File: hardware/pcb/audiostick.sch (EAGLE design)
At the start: 65 parts, among them IC1 TPS73633MBDV, IC3 PCM5102ASW, IC5 AP22804W5, IC6 TINY13V-10SSU, J2 AUDIO_JACK_3.5MM_PTH, J3 USB-B, SW1 EVQP7, T1 BC850

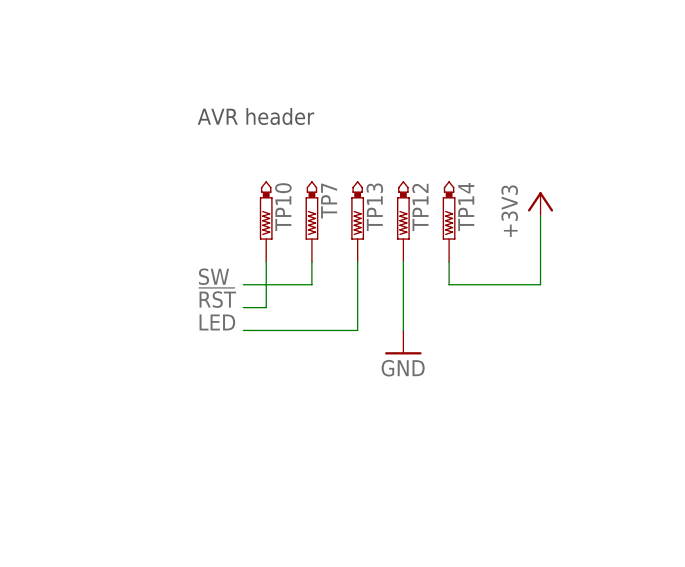
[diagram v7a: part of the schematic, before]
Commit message: Changed pogo points for proper header, silly idea!
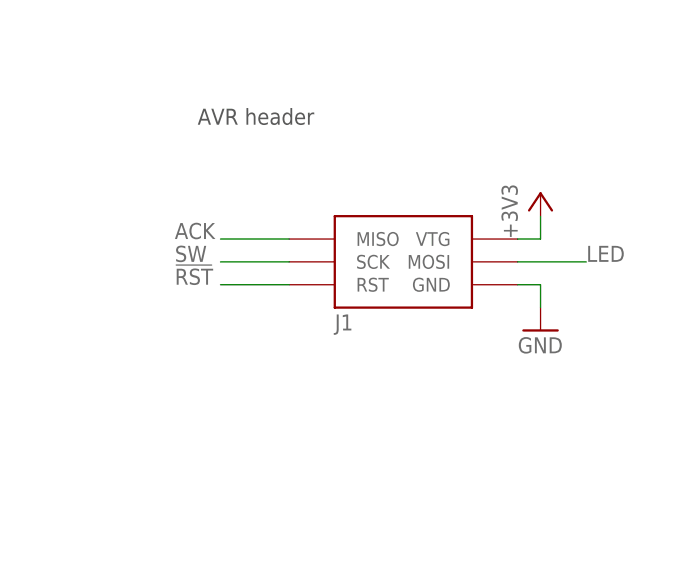
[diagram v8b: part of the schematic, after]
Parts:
- removed TP10, TP12, TP13, TP14, TP7: PTR1TP08R, testpad:PTR1TP08R
- added J1: AVRISP6TH127, AWJLEagleLib:AVRISP6TH127
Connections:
- net !RST: now also J1.RST; no longer TP10.TP
- net +3V3: now also J1.VTG; no longer TP14.TP
- net ACK: now also J1.MISO
- net GND: now also J1.GND; no longer TP12.TP
- net LED: now also J1.MOSI; no longer TP13.TP
- net SW: now also J1.SCK; no longer TP7.TP
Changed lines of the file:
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@@
 <part name="R13" library="rcl" library_urn="urn:adsk.eagle:library:334" deviceset="R-EU_" device="R0603" package3d_urn="urn:adsk.eagle:package:23555/3" value="10K"/>
 <part name="IC6" library="atmel" library_urn="urn:adsk.eagle:library:105" deviceset="TINY13" device="SSU" package3d_urn="urn:adsk.eagle:package:4358/1" technology="V-10"/>
-<part name="+3V5" library="supply1" library_urn="urn:adsk.eagle:library:371" deviceset="+3V3" device=""/>
-<part name="GND19" library="supply1" library_urn="urn:adsk.eagle:library:371" deviceset="GND" device=""/>
 <part name="TP1" library="testpad" library_urn="urn:adsk.eagle:library:385" deviceset="PTR1" device="PAD1-13" package3d_urn="urn:adsk.eagle:package:27946/1"/>
 <part name="TP2" library="testpad" library_urn="urn:adsk.eagle:library:385" deviceset="PTR1" device="PAD1-13" package3d_urn="urn:adsk.eagle:package:27946/1"/>
@@
 <part name="R8" library="rcl" library_urn="urn:adsk.eagle:library:334" deviceset="R-EU_" device="R0603" package3d_urn="urn:adsk.eagle:package:23555/3" value="0R"/>
 <part name="SW1" library="AudioStick" deviceset="EVQP7" device=""/>
-<part name="TP7" library="testpad" library_urn="urn:adsk.eagle:library:385" deviceset="PTR1" device="TP08R" package3d_urn="urn:adsk.eagle:package:27956/1" value="PTR1TP08R"/>
-<part name="TP10" library="testpad" library_urn="urn:adsk.eagle:library:385" deviceset="PTR1" device="TP08R" package3d_urn="urn:adsk.eagle:package:27956/1" value="PTR1TP08R"/>
-<part name="TP12" library="testpad" library_urn="urn:adsk.eagle:library:385" deviceset="PTR1" device="TP08R" package3d_urn="urn:adsk.eagle:package:27956/1" value="PTR1TP08R"/>
-<part name="TP13" library="testpad" library_urn="urn:adsk.eagle:library:385" deviceset="PTR1" device="TP08R" package3d_urn="urn:adsk.eagle:package:27956/1" value="PTR1TP08R"/>
-<part name="TP14" library="testpad" library_urn="urn:adsk.eagle:library:385" deviceset="PTR1" device="TP08R" package3d_urn="urn:adsk.eagle:package:27956/1" value="PTR1TP08R"/>
+<part name="J1" library="AWJLEagleLib" deviceset="AVRISP6" device="TH127"/>
+<part name="+3V7" library="supply1" library_urn="urn:adsk.eagle:library:371" deviceset="+3V3" device=""/>
+<part name="GND28" library="supply1" library_urn="urn:adsk.eagle:library:371" deviceset="GND" device=""/>
 </parts>
 <sheets>
@@
 <attribute name="VALUE" x="55.88" y="327.66" size="1.778" layer="96" rot="MR0"/>
 </instance>
-<instance part="+3V5" gate="G$1" x="238.76" y="353.06" smashed="yes">
-<attribute name="VALUE" x="236.22" y="347.98" size="1.778" layer="96" rot="R90"/>
-</instance>
-<instance part="GND19" gate="1" x="223.52" y="335.28" smashed="yes">
-<attribute name="VALUE" x="220.98" y="332.74" size="1.778" layer="96"/>
-</instance>
 <instance part="TP1" gate="G$1" x="147.32" y="88.9" smashed="yes" rot="R90">
 <attribute name="NAME" x="153.67" y="87.884" size="1.778" layer="95" rot="R180"/>
@@
 <attribute name="VALUE" x="80.01" y="325.755" size="1.778" layer="96" rot="R90"/>
 </instance>
-<instance part="TP7" gate="G$1" x="213.36" y="347.98" smashed="yes" rot="R180">
-<attribute name="NAME" x="214.376" y="354.33" size="1.778" layer="95" rot="R270"/>
-<attribute name="TP_SIGNAL_NAME" x="212.09" y="350.52" size="1.778" layer="97" rot="R180"/>
-</instance>
-<instance part="TP10" gate="G$1" x="208.28" y="347.98" smashed="yes" rot="R180">
-<attribute name="NAME" x="209.296" y="354.33" size="1.778" layer="95" rot="R270"/>
-<attribute name="TP_SIGNAL_NAME" x="207.01" y="350.52" size="1.778" layer="97" rot="R180"/>
-</instance>
-<instance part="TP12" gate="G$1" x="223.52" y="347.98" smashed="yes" rot="R180">
-<attribute name="NAME" x="224.536" y="354.33" size="1.778" layer="95" rot="R270"/>
-<attribute name="TP_SIGNAL_NAME" x="222.25" y="350.52" size="1.778" layer="97" rot="R180"/>
-</instance>
-<instance part="TP13" gate="G$1" x="218.44" y="347.98" smashed="yes" rot="R180">
-<attribute name="NAME" x="219.456" y="354.33" size="1.778" layer="95" rot="R270"/>
-<attribute name="TP_SIGNAL_NAME" x="217.17" y="350.52" size="1.778" layer="97" rot="R180"/>
-</instance>
-<instance part="TP14" gate="G$1" x="228.6" y="347.98" smashed="yes" rot="R180">
-<attribute name="NAME" x="229.616" y="354.33" size="1.778" layer="95" rot="R270"/>
-<attribute name="TP_SIGNAL_NAME" x="227.33" y="350.52" size="1.778" layer="97" rot="R180"/>
+<instance part="J1" gate="G$1" x="223.52" y="345.44" smashed="yes">
+<attribute name="NAME" x="215.9" y="337.82" size="1.778" layer="95"/>
+</instance>
+<instance part="+3V7" gate="G$1" x="238.76" y="353.06" smashed="yes">
+<attribute name="VALUE" x="236.22" y="347.98" size="1.778" layer="96" rot="R90"/>
+</instance>
+<instance part="GND28" gate="1" x="238.76" y="337.82" smashed="yes">
+<attribute name="VALUE" x="236.22" y="335.28" size="1.778" layer="96"/>
 </instance>
 </instances>
@@
 </segment>
 <segment>
-<pinref part="GND19" gate="1" pin="GND"/>
-<pinref part="TP12" gate="G$1" pin="TP"/>
-<wire x1="223.52" y1="337.82" x2="223.52" y2="345.44" width="0.1524" layer="91"/>
-</segment>
-<segment>
 <pinref part="TP8" gate="G$1" pin="TP"/>
 <wire x1="139.7" y1="40.64" x2="139.7" y2="38.1" width="0.1524" layer="91"/>
@@
 <wire x1="129.54" y1="335.28" x2="129.54" y2="337.82" width="0.1524" layer="91"/>
 </segment>
+<segment>
+<pinref part="J1" gate="G$1" pin="GND"/>
+<pinref part="GND28" gate="1" pin="GND"/>
+<wire x1="236.22" y1="342.9" x2="238.76" y2="342.9" width="0.1524" layer="91"/>
+<wire x1="238.76" y1="342.9" x2="238.76" y2="340.36" width="0.1524" layer="91"/>
+</segment>
 </net>
 <net name="PWR" class="0">
@@
 </segment>
 <segment>
-<pinref part="+3V5" gate="G$1" pin="+3V3"/>
-<wire x1="228.6" y1="342.9" x2="238.76" y2="342.9" width="0.1524" layer="91"/>
-<wire x1="238.76" y1="342.9" x2="238.76" y2="350.52" width="0.1524" layer="91"/>
-<pinref part="TP14" gate="G$1" pin="TP"/>
-<wire x1="228.6" y1="345.44" x2="228.6" y2="342.9" width="0.1524" layer="91"/>
-</segment>
-<segment>
 <pinref part="R14" gate="G$1" pin="2"/>
 <pinref part="+3V6" gate="G$1" pin="+3V3"/>
@@
 <wire x1="129.54" y1="375.92" x2="129.54" y2="378.46" width="0.1524" layer="91"/>
 </segment>
+<segment>
+<pinref part="J1" gate="G$1" pin="VTG"/>
+<pinref part="+3V7" gate="G$1" pin="+3V3"/>
+<wire x1="236.22" y1="347.98" x2="238.76" y2="347.98" width="0.1524" layer="91"/>
+<wire x1="238.76" y1="347.98" x2="238.76" y2="350.52" width="0.1524" layer="91"/>
+</segment>
 </net>
 <net name="!RST" class="0">
-<segment>
-<label x="200.66" y="340.36" size="1.778" layer="95"/>
-<pinref part="TP10" gate="G$1" pin="TP"/>
-<wire x1="208.28" y1="340.36" x2="205.74" y2="340.36" width="0.1524" layer="91"/>
-<wire x1="208.28" y1="345.44" x2="208.28" y2="340.36" width="0.1524" layer="91"/>
-</segment>
 <segment>
 <pinref part="IC6" gate="G$1" pin="PB5/PCINT5/!RESET!/ADC0/DW"/>
@@
 <wire x1="73.66" y1="335.28" x2="73.66" y2="358.14" width="0.1524" layer="91"/>
 <label x="76.2" y="335.28" size="1.778" layer="95"/>
+</segment>
+<segment>
+<pinref part="J1" gate="G$1" pin="RST"/>
+<wire x1="210.82" y1="342.9" x2="203.2" y2="342.9" width="0.1524" layer="91"/>
+<label x="198.12" y="342.9" size="1.778" layer="95"/>
 </segment>
 </net>
@@
 </segment>
 <segment>
-<label x="200.66" y="342.9" size="1.778" layer="95"/>
-<pinref part="TP7" gate="G$1" pin="TP"/>
-<wire x1="213.36" y1="342.9" x2="205.74" y2="342.9" width="0.1524" layer="91"/>
-<wire x1="213.36" y1="345.44" x2="213.36" y2="342.9" width="0.1524" layer="91"/>
+<pinref part="J1" gate="G$1" pin="SCK"/>
+<wire x1="210.82" y1="345.44" x2="203.2" y2="345.44" width="0.1524" layer="91"/>
+<label x="198.12" y="345.44" size="1.778" layer="95"/>
 </segment>
 </net>
@@
 <wire x1="157.48" y1="175.26" x2="157.48" y2="177.8" width="0.1524" layer="91"/>
 <junction x="157.48" y="177.8"/>
+</segment>
+<segment>
+<pinref part="J1" gate="G$1" pin="MISO"/>
+<wire x1="210.82" y1="347.98" x2="203.2" y2="347.98" width="0.1524" layer="91"/>
+<label x="198.12" y="347.98" size="1.778" layer="95"/>
 </segment>
 </net>
@@
 </segment>
 <segment>
-<wire x1="205.74" y1="337.82" x2="218.44" y2="337.82" width="0.1524" layer="91"/>
-<label x="200.66" y="337.82" size="1.778" layer="95"/>
-<pinref part="TP13" gate="G$1" pin="TP"/>
-<wire x1="218.44" y1="337.82" x2="218.44" y2="345.44" width="0.1524" layer="91"/>
-</segment>
-</net>
+<pinref part="J1" gate="G$1" pin="MOSI"/>
+<wire x1="236.22" y1="345.44" x2="243.84" y2="345.44" width="0.1524" layer="91"/>
+<label x="243.84" y="345.44" size="1.778" layer="95"/>
+</segment>
+</net>
